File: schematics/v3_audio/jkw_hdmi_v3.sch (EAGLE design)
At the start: 50 parts, among them J1 2X20-CHIP-HEADERS, J3 T_MOLEX_45171, Q2 12mhz, U1 DS2431P, U2 LP5907MFX

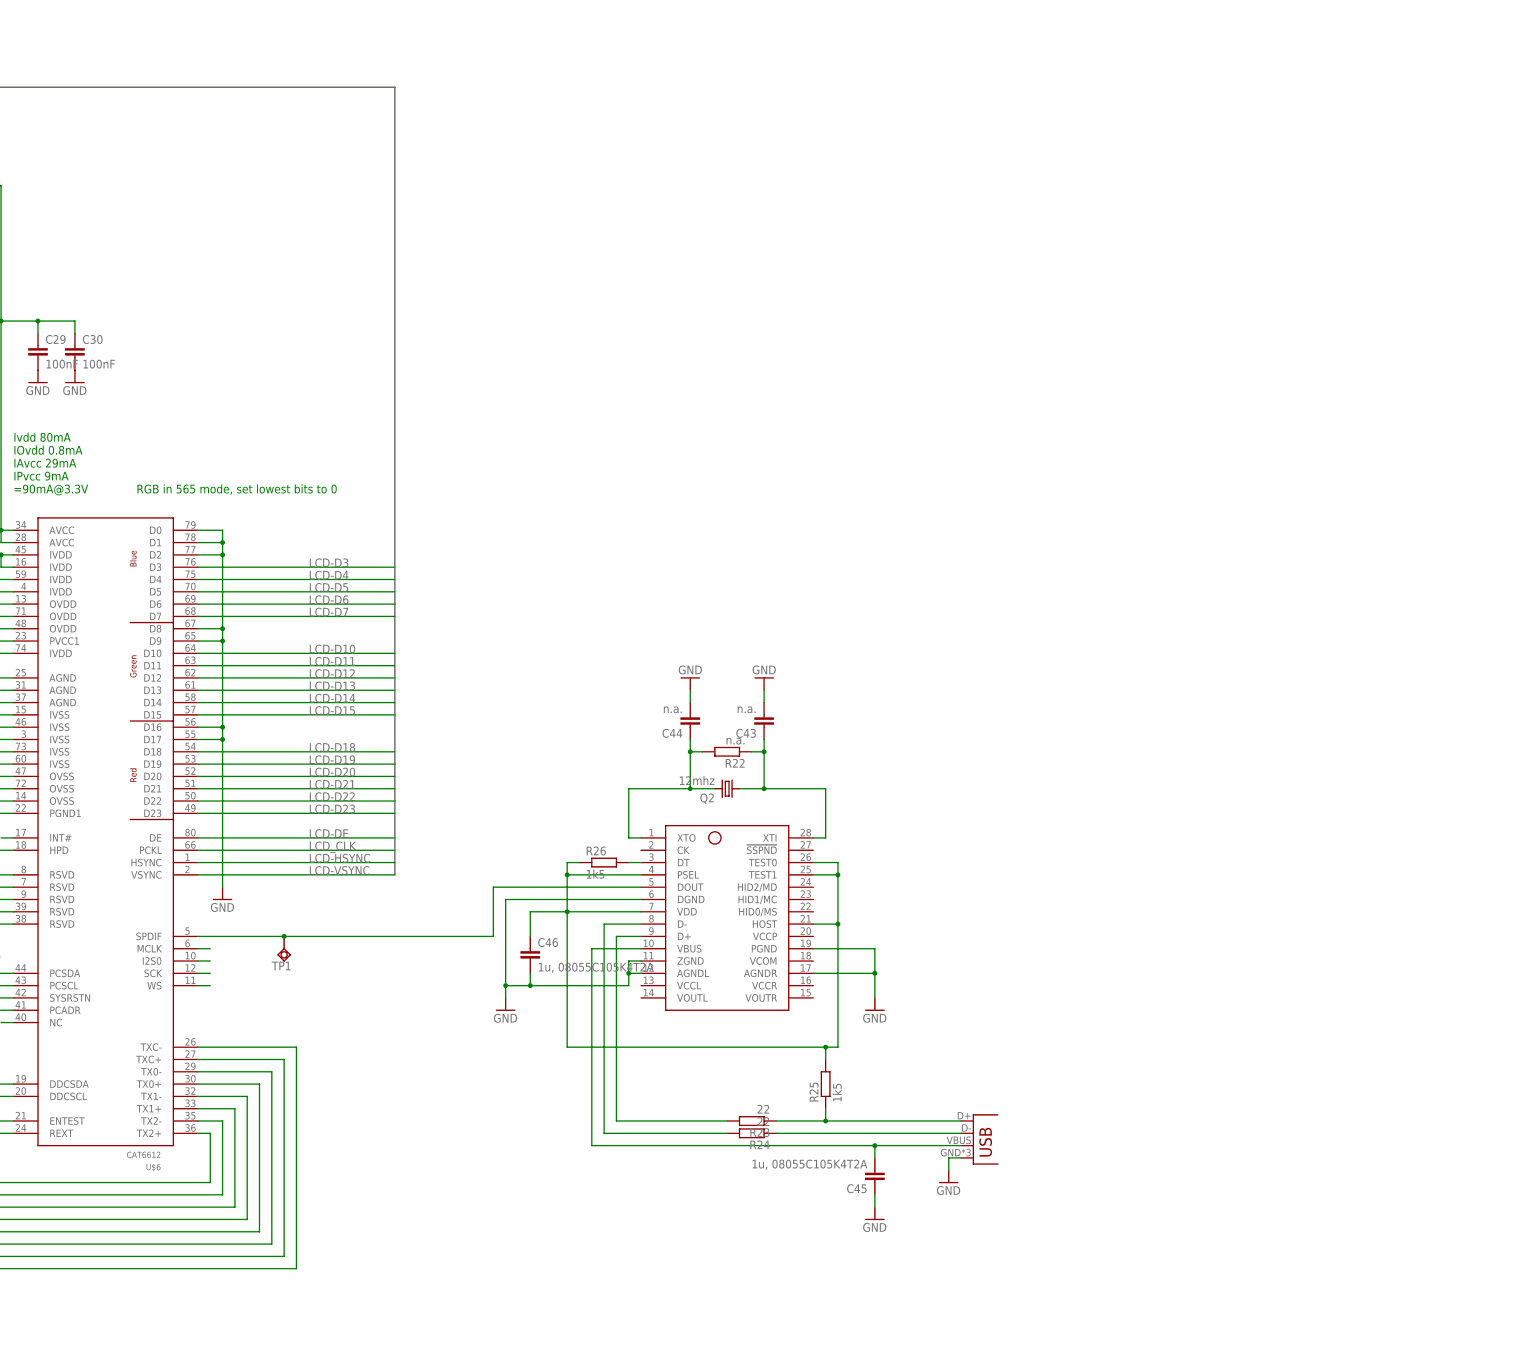
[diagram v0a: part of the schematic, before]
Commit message: updated routing for LCD length matching
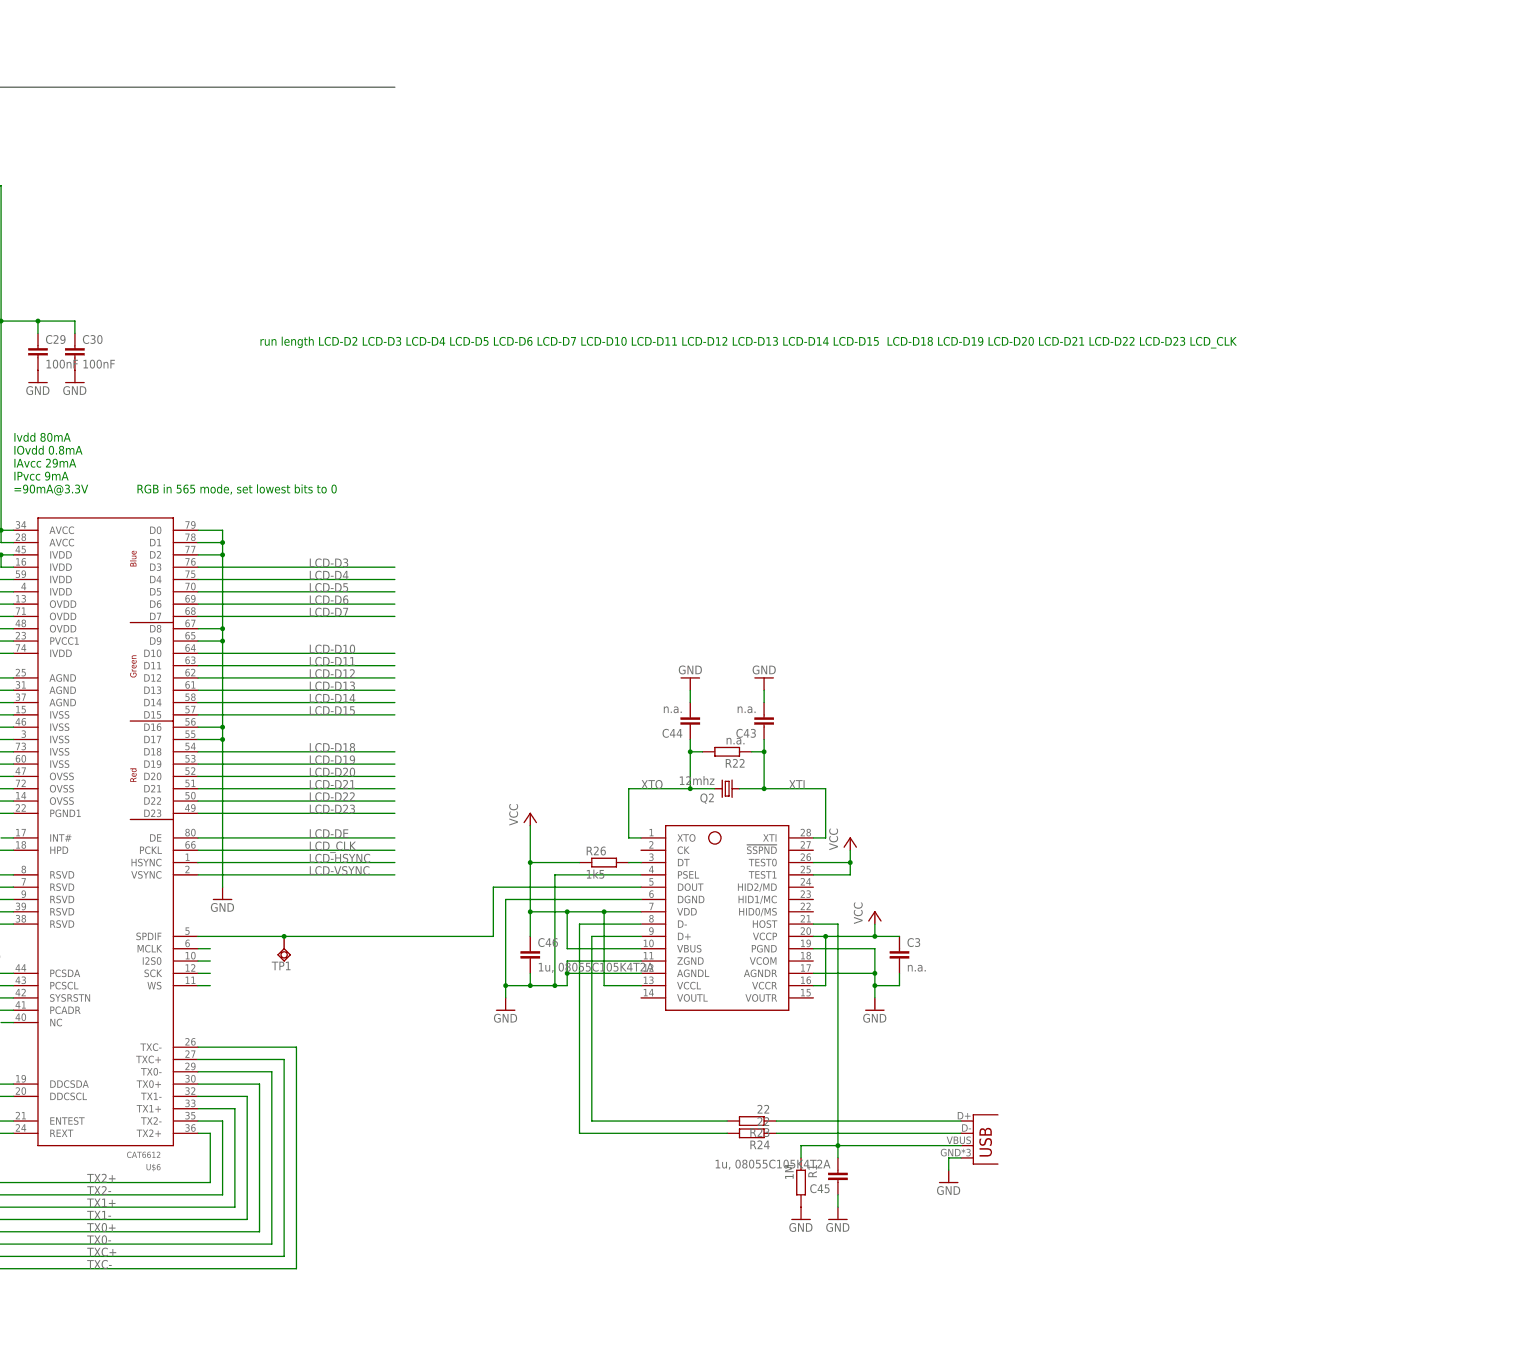
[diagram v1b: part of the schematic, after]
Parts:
- removed R25: 1k5, rcl:R-EU_M0805
- added C3: n.a., rcl:C-EUC0805
- added R1: 1M, rcl:R-EU_M0805
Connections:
- net N$11 renamed TXC-
- net N$14 renamed TXC+
- net N$15 renamed TX2+
- net N$16 renamed TX2-
- net N$17 renamed TX1+
- net N$18 renamed TX1-
- net N$19 renamed TX0+
- net N$20 renamed TX0-
- net N$57 renamed XTO
- net N$58 renamed XTI
- removed net N$66: AUDIO_USB.VBUS, C45.2, U$5.VBUS
- net GND: now also C3.2, R1.2, U$5.PSEL
- net N$62: no longer R25.1
- net VCC: now also C3.1, C46.1, R26.1, U$5.TEST0, U$5.TEST1, U$5.VBUS, U$5.VCCL, U$5.VCCP, U$5.VCCR, U$5.VDD
- net VCC2: now also AUDIO_USB.VBUS, C45.2, R1.1; no longer C46.1, R25.2, R26.1, U$5.PSEL, U$5.TEST0, U$5.TEST1, U$5.VDD
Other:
- note added: "run length LCD-D2 LCD-D3 LCD-D4 LCD-D5 LCD-D6 LCD-D7 LCD-D10 LCD-D11 LCD-D12 LCD-D13 LCD-D14 LCD-D15 LCD-D18 LCD-D19 LCD-D20 LCD-D21 LCD-D22 LCD-D23 LCD_CLK"
- moved on the sheet: C45

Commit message: added frame
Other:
- moved on the sheet: C3, C43, C44, C45, C46, D6, GND, J1, JP1, Q2, R1, R19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

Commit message: minor fixes
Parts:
- J1: device VGA-DIP:2X20-CHIP-HEADERS -> JKW_CHIP:2X20-CHIP-HEADERS
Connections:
- net N$12 renamed ACIN
- net N$5 renamed LCD-D2

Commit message: ?
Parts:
- U2: value LP5907MFX -> LP5907MFX-1.8
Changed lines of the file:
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@@
 <part name="D1" library="diode" deviceset="BAS40" device=""/>
 <part name="GND40" library="supply1" deviceset="GND" device=""/>
-<part name="U2" library="JKW_CHIP" deviceset="LP5907MFX" device=""/>
+<part name="U2" library="JKW_CHIP" deviceset="LP5907MFX" device="" value="LP5907MFX-1.8"/>
 <part name="C27" library="rcl" deviceset="C-EU" device="C0805" value="1u"/>
 <part name="C28" library="rcl" deviceset="C-EU" device="C0805" value="1u"/>
